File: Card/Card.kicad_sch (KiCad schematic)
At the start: 9 parts, among them U1 MAX7219, U2 MAX7219, U3 MAX7219, U4 MAX7219, U5 MAX7219

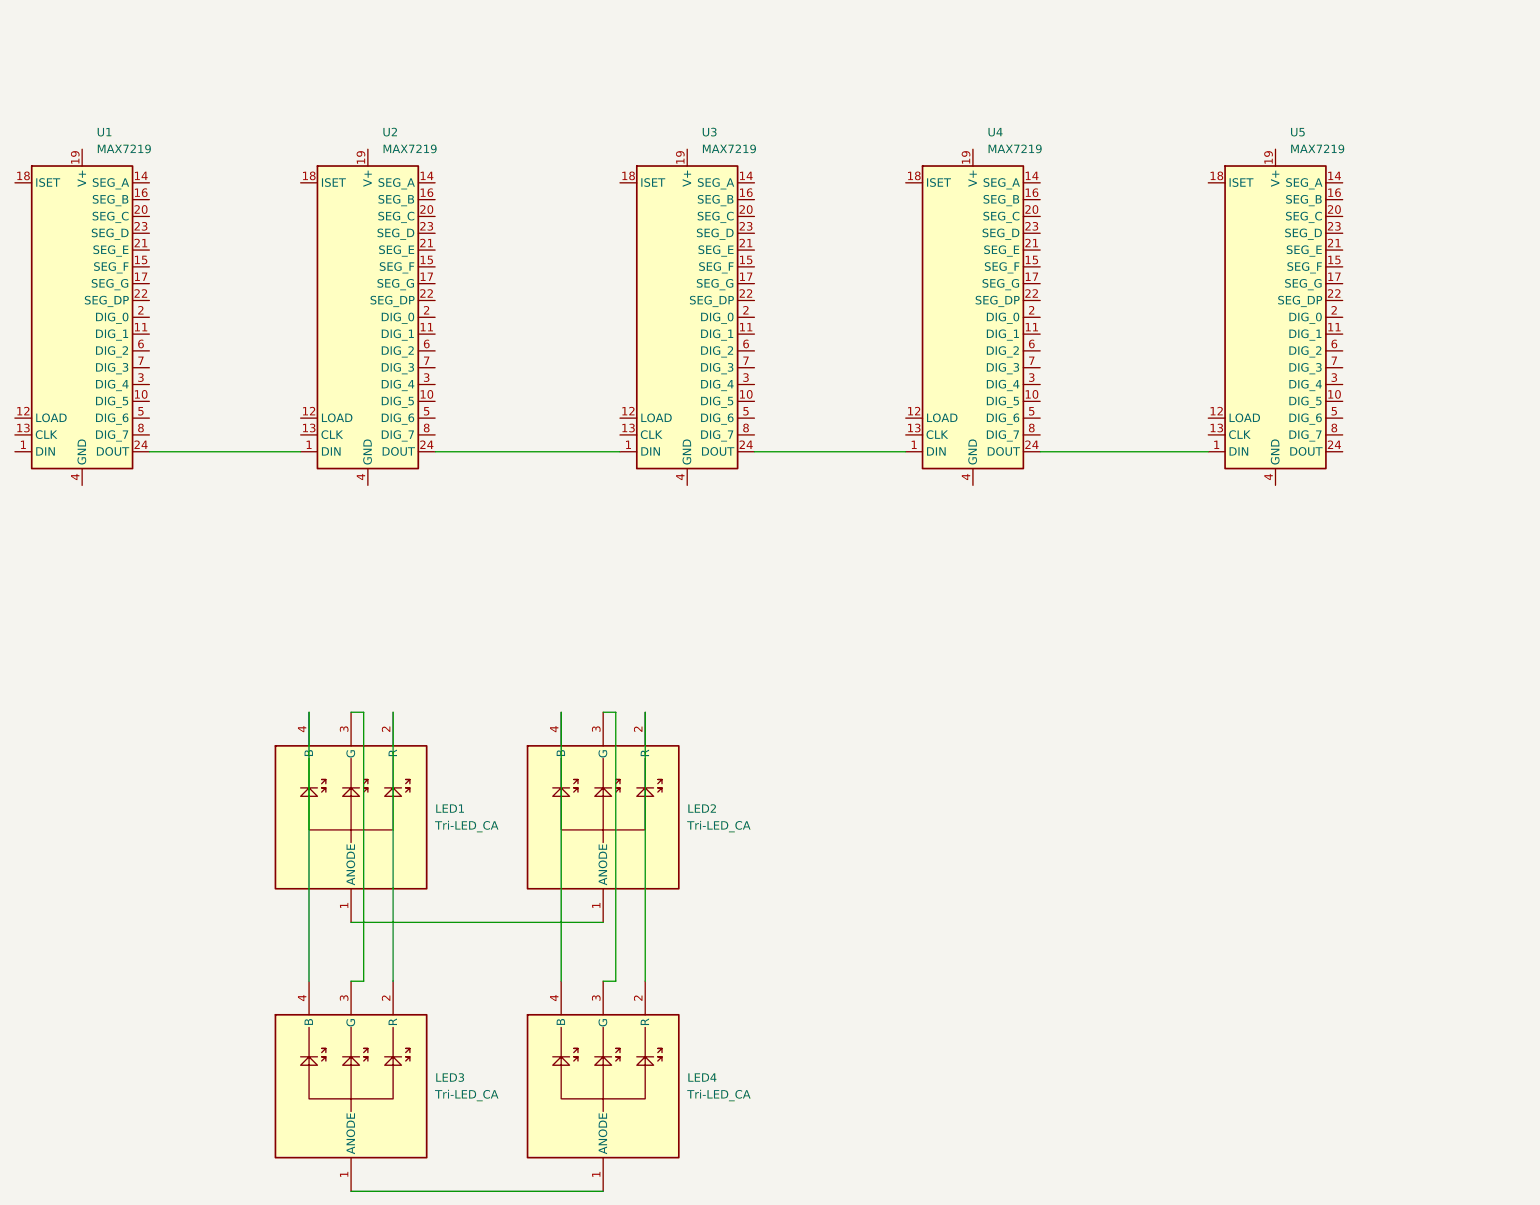
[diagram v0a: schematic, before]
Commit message: created LED matrix
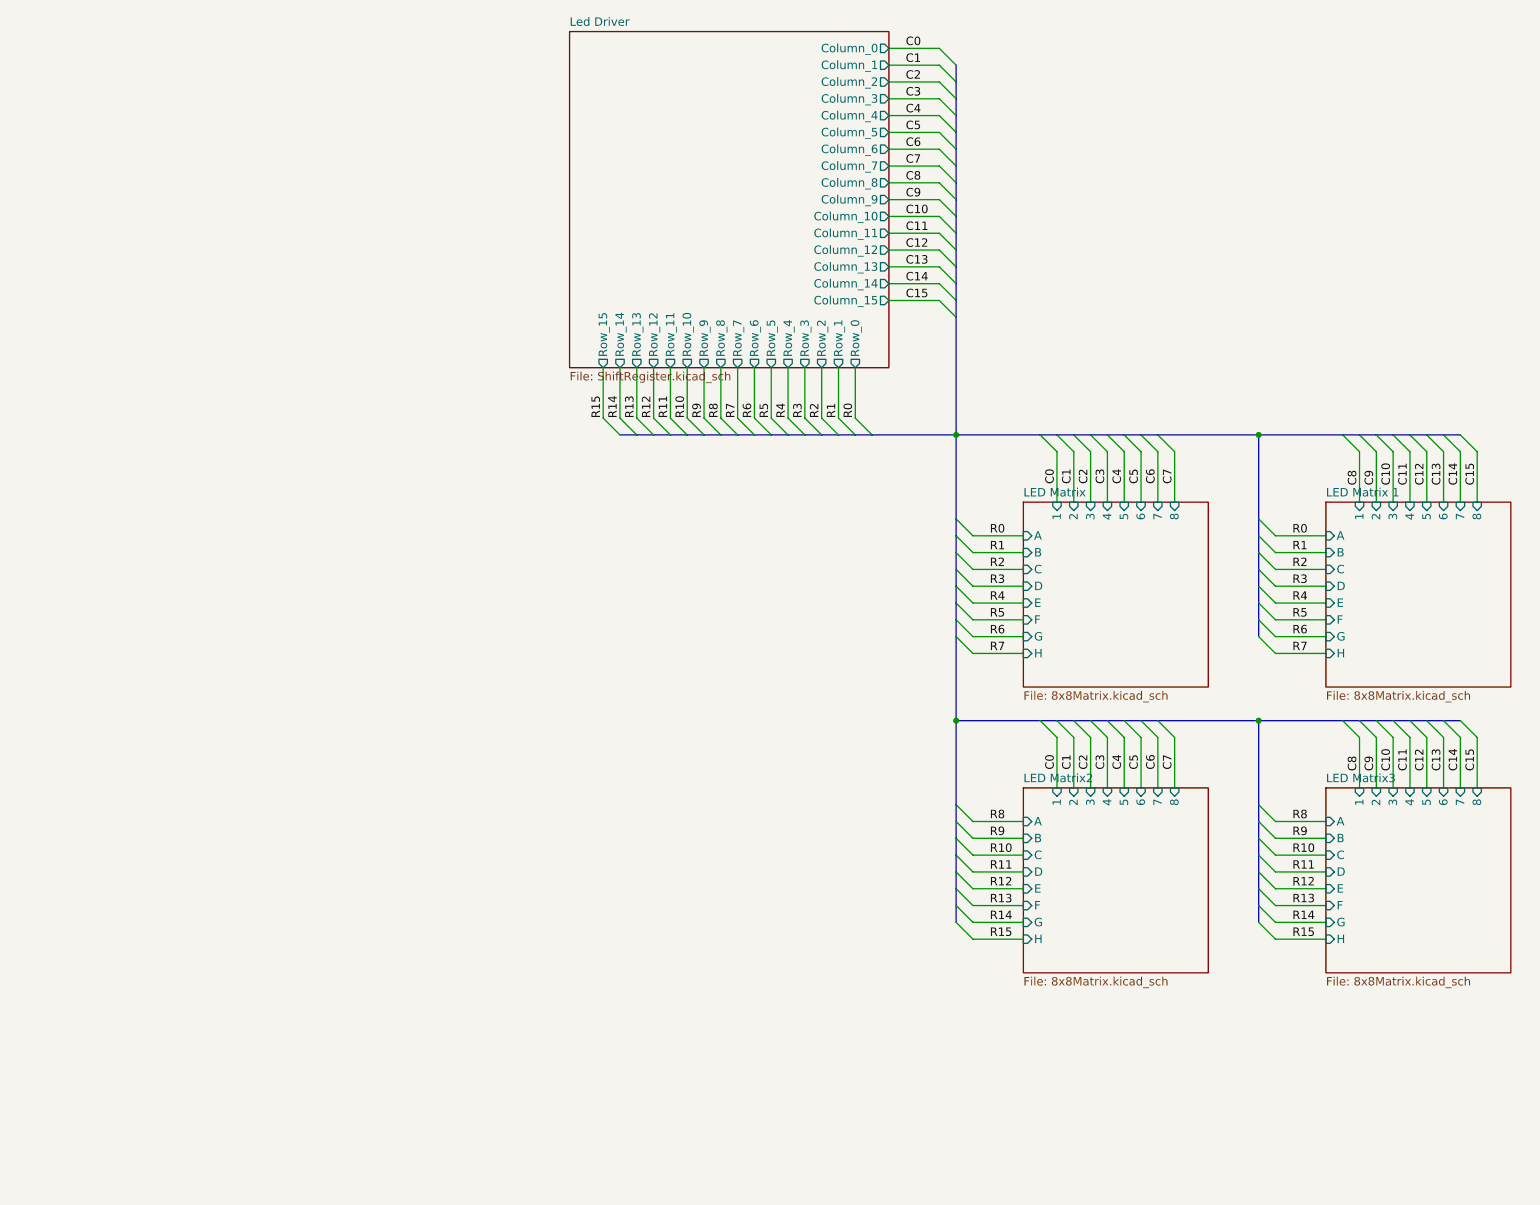
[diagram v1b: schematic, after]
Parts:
- removed LED1, LED2, LED3, LED4: Tri-LED_CA, Footprints:LED_Cree-PLCC4_3.2x2.8mm_CCW, symbol Custom:Tri-LED_CA
- removed U1, U2, U3, U4, U5: MAX7219, symbol Driver_LED:MAX7219
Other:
- added sheet LED Matrix (8x8Matrix.kicad_sch)
- added sheet LED Matrix 1 (8x8Matrix.kicad_sch)
- added sheet LED Matrix2 (8x8Matrix.kicad_sch)
- added sheet LED Matrix3 (8x8Matrix.kicad_sch)
- added sheet Led Driver (ShiftRegister.kicad_sch)
